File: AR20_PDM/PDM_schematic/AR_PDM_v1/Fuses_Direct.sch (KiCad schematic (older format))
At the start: 9 parts, among them U31 INA233

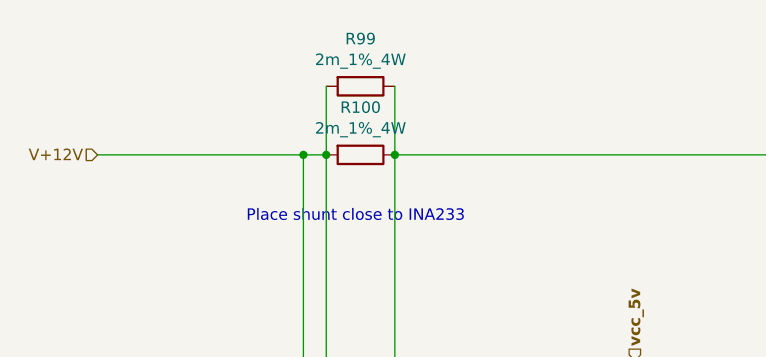
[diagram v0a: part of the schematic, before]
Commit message: Fixed wrong resistors, mos sense. Gerber files updated
- removed all R_is_protection resistors on each mosfet line
- added one R_is_protection resistors to mos_sense_all
ps, mux N-fets, does not need overvoltage protection. 60 volt tolerant.
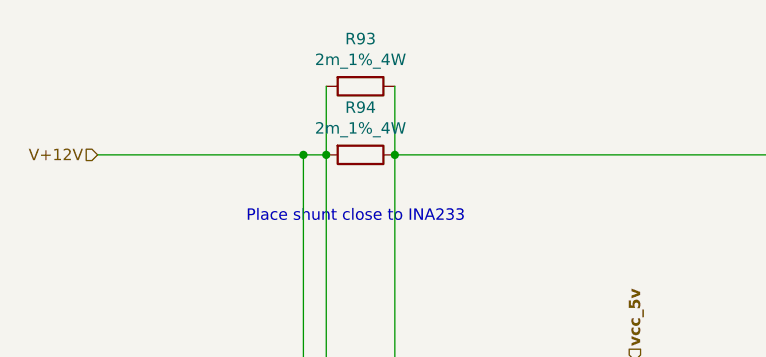
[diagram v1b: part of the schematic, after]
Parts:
- renumbered R99 to R93, R100 to R94
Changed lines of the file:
@@
 AR Path="/5E0FDCCC/5E1E306F" Ref="R?"  Part="1"
 AR Path="/5E10174B/5E1E306F" Ref="R?"  Part="1"
-AR Path="/5DE4D361/5E1E306F" Ref="R100"  Part="1"
-F 0 "R100" V 3243 3000 50  0000 C CNN
+AR Path="/5DE4D361/5E1E306F" Ref="R94"  Part="1"
+F 0 "R94" V 3243 3000 50  0000 C CNN
 F 1 "2m_1%_4W" V 3334 3000 50  0000 C CNN
 F 2 "Resistor_SMD:R_2512_6332Metric" V 3380 3000 50  0001 C CNN
@@
 AR Path="/5E0FDCCC/5E24C0CF" Ref="R?"  Part="1"
 AR Path="/5E10174B/5E24C0CF" Ref="R?"  Part="1"
-AR Path="/5DE4D361/5E24C0CF" Ref="R99"  Part="1"
-F 0 "R99" V 3243 2700 50  0000 C CNN
+AR Path="/5DE4D361/5E24C0CF" Ref="R93"  Part="1"
+F 0 "R93" V 3243 2700 50  0000 C CNN
 F 1 "2m_1%_4W" V 3334 2700 50  0000 C CNN
 F 2 "Resistor_SMD:R_2512_6332Metric" V 3380 2700 50  0001 C CNN

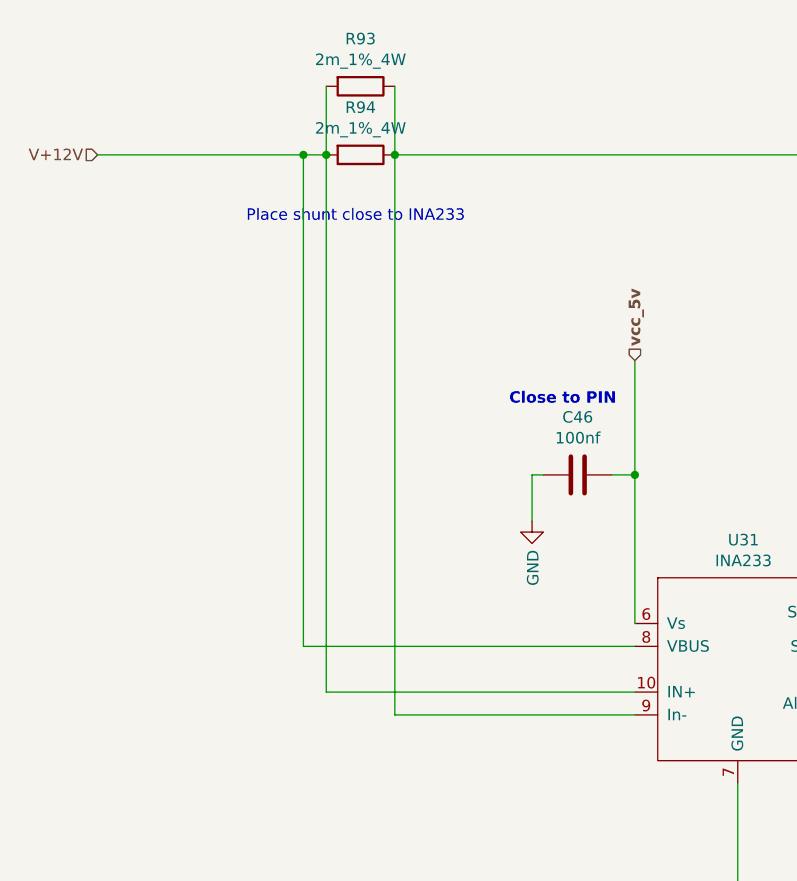
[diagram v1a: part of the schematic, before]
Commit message: Major redesign. schematics completed, PCB work in progress
-TODO : A proper changelog file. Where all changes will apear 
- Redesigned schematics to accommodate errors in the improvement list
- More detail in ALPHA improvement list
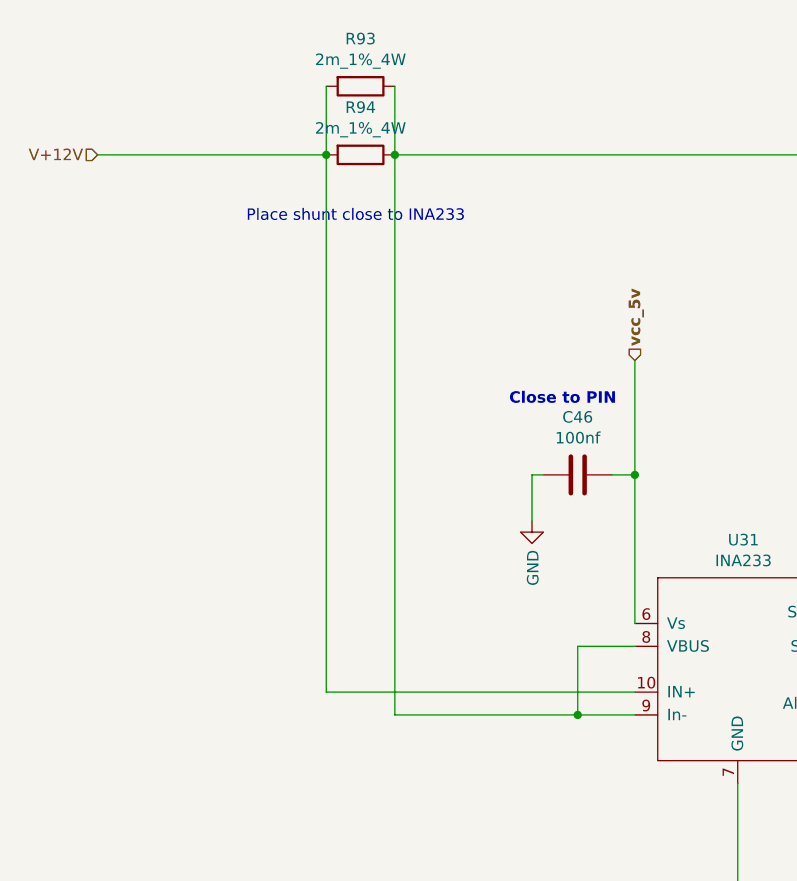
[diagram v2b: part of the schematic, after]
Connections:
- net V+12V: no longer U31.8 (VBUS)
- net at F1.2, F2.2, F3.2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: now also U31.8 (VBUS)
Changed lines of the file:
@@
 $Descr A4 11693 8268
 encoding utf-8
-Sheet 13 13
+Sheet 12 14
 Title ""
 Date ""
@@
 Place shunt close to INA233\n
 Wire Wire Line
-	2300 3000 3200 3000
-Wire Wire Line
 	5950 2650 5950 2950
 Wire Wire Line
@@
 Wire Wire Line
 	4650 5350 3300 5350
-Wire Wire Line
-	3600 5450 4650 5450
-Wire Wire Line
-	3200 5150 3200 3000
-Wire Wire Line
-	3200 5150 4650 5150
-Connection ~ 3200 3000
 Text HLabel 8950 3550 2    50   Output ~ 0
 SHUTDOWN_OUT
@@
 Connection ~ 3600 3000
 Wire Wire Line
-	3200 3000 3300 3000
-Wire Wire Line
 	3300 3000 3300 5350
 Connection ~ 3300 3000
@@
 Wire Wire Line
 	3600 3000 3600 2700
+Wire Wire Line
+	2300 3000 3300 3000
+Wire Wire Line
+	4650 5150 4400 5150
+Wire Wire Line
+	4400 5150 4400 5450
+Wire Wire Line
+	3600 5450 4400 5450
+Connection ~ 4400 5450
+Wire Wire Line
+	4400 5450 4650 5450
 $EndSCHEMATC

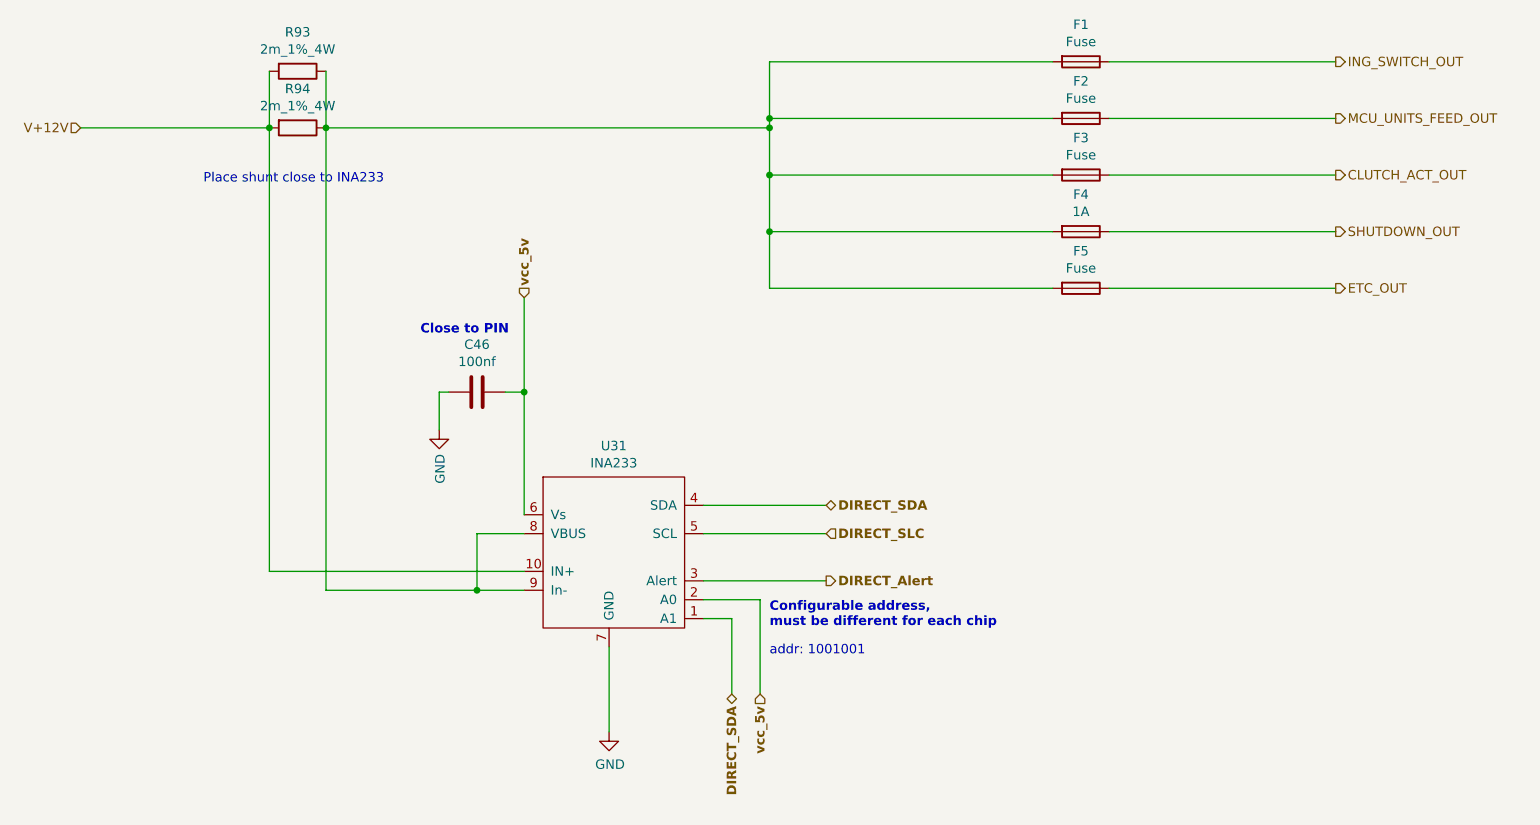
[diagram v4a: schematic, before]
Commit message: schematics rework
Fixed INA233 frying due to inductive flyback:
- Paced ina233 high side of the mosftets
- New input protection reseistors, and zener diodes, on each ina233.
Simplified:
- Removed the MUX and mos sense lines, as i realize that most of this functionality can be obtained trough INA233.
- Removed some of the cappacitors , besides the most needed ones.
- removed  back to back zener diode configuration, now a single diode insted.
 to reduce negative voltage in case of loss of VS, to be easy on the INA233 filters.
new stuff:
- Another temp sensor.
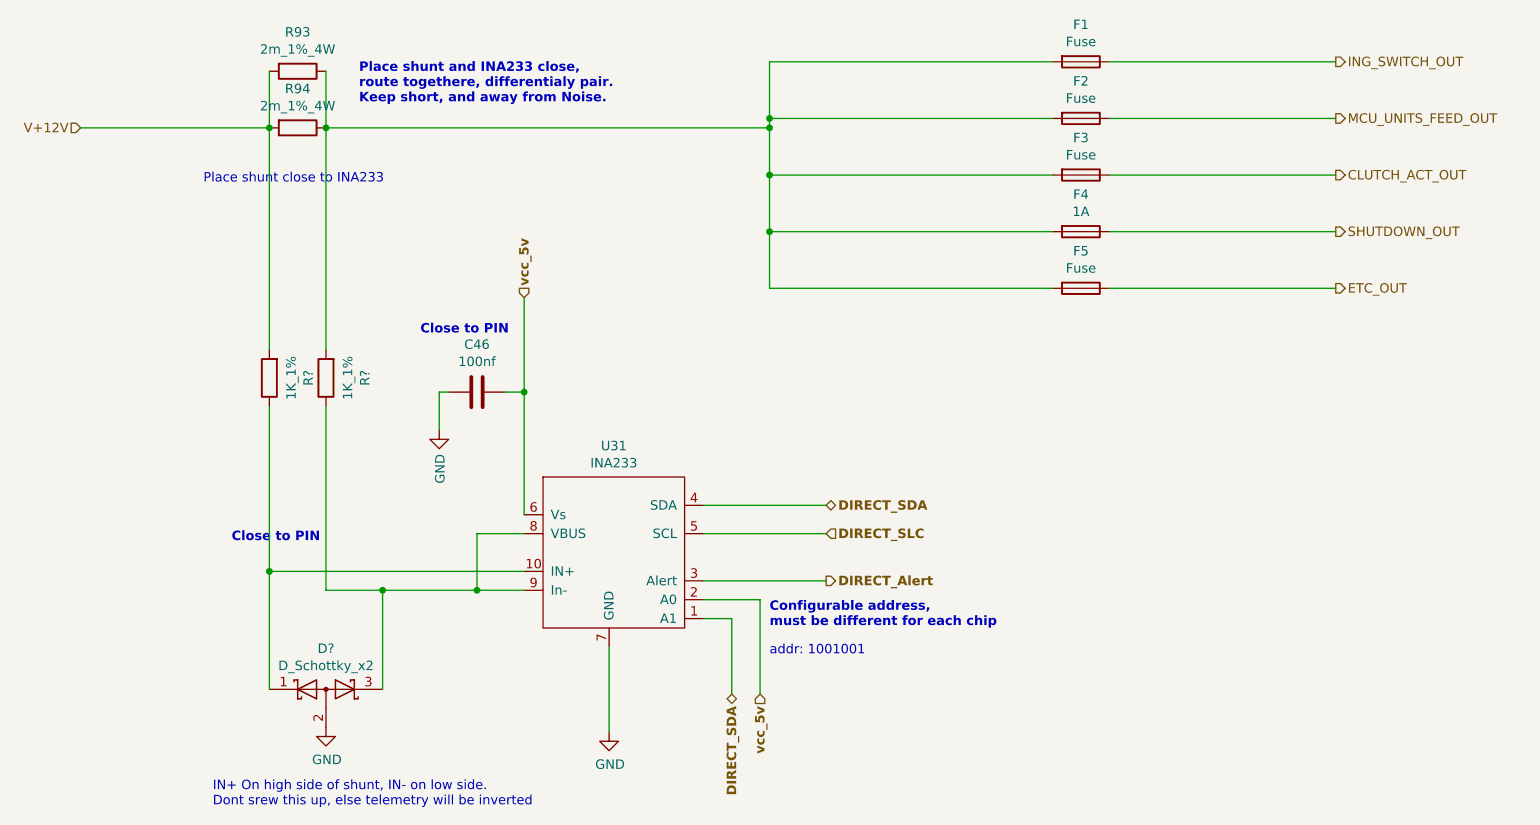
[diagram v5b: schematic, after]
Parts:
- added D?: D_Schottky_x2, symbol AR20_PDM_v1-rescue:D_Schottky_x2
- added R? (x2): 1K_1%, Resistor_SMD:R_0603_1608Metric, symbol AR20_PDM_v1-rescue:R-Device
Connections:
- net GND: now also D?.2 (A)
- net V+12V: now also R?.2; no longer U31.10 (IN+)
- net at F1.2, F2.2, F3.2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: now also R?.2; no longer U31.8 (VBUS), U31.9 (In-)
- new net: D?.1 (K), R?.1, U31.10 (IN+)
- new net: D?.3 (K), R?.1, U31.8 (VBUS), U31.9 (In-)
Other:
- note added: "IN+ On high side of shunt, IN- on low side.\nDont srew this up, else telemetry will be inverted"
- note added: "Place shunt and INA233 close, \nroute togethere, differentialy pair. \nKeep short, and away from Noise."
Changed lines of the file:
@@
 $Descr A4 11693 8268
 encoding utf-8
-Sheet 11 14
+Sheet 10 13
 Title ""
 Date ""
@@
 $EndComp
 Wire Wire Line
-	3600 3000 3600 5450
-Wire Wire Line
 	3600 3000 5950 3000
 Connection ~ 3600 3000
-Wire Wire Line
-	3300 3000 3300 5350
 Connection ~ 3300 3000
 Text Notes 5950 5800 0    50   ~ 0
@@
 	4400 5150 4400 5450
 Wire Wire Line
-	3600 5450 4400 5450
+	3600 5450 3900 5450
 Connection ~ 4400 5450
 Wire Wire Line
 	4400 5450 4650 5450
+Text Notes 3100 5200 0    50   ~ 10
+Close to PIN
+$Comp
+L AR20_PDM_v1-rescue:D_Schottky_x2 D?
+U 1 1 5EED49C1
+P 3600 5975
+AR Path="/5DA89415/5EED49C1" Ref="D?"  Part="1"
+AR Path="/5E10174B/5EED49C1" Ref="D?"  Part="1"
+F 0 "D?" H 3600 6191 50  0000 C CNN
+F 1 "D_Schottky_x2" H 3600 6100 50  0000 C CNN
+F 2 "" H 3600 5975 50  0001 C CNN
+F 3 "~" H 3600 5975 50  0001 C CNN
+	1    3600 5975
+	1    0    0    -1
+$EndComp
+$Comp
+L AR20_PDM_v1-rescue:GND-power #PWR?
+U 1 1 5EED49DB
+P 3600 6175
+AR Path="/5DA89415/5EED49DB" Ref="#PWR?"  Part="1"
+AR Path="/5DEB10A1/5EED49DB" Ref="#PWR?"  Part="1"
+AR Path="/5DEB20EA/5EED49DB" Ref="#PWR?"  Part="1"
+AR Path="/5E0E4725/5EED49DB" Ref="#PWR?"  Part="1"
+AR Path="/5E0E4A93/5EED49DB" Ref="#PWR?"  Part="1"
+AR Path="/5E0E4EB5/5EED49DB" Ref="#PWR?"  Part="1"
+AR Path="/5E0E5304/5EED49DB" Ref="#PWR?"  Part="1"
+AR Path="/5E0E594B/5EED49DB" Ref="#PWR?"  Part="1"
+AR Path="/5E0E607C/5EED49DB" Ref="#PWR?"  Part="1"
+AR Path="/5E0FB5C8/5EED49DB" Ref="#PWR?"  Part="1"
+AR Path="/5E0FBBBD/5EED49DB" Ref="#PWR?"  Part="1"
+AR Path="/5E0FC3A2/5EED49DB" Ref="#PWR?"  Part="1"
+AR Path="/5E0FCFDC/5EED49DB" Ref="#PWR?"  Part="1"
+AR Path="/5E0FDCCC/5EED49DB" Ref="#PWR?"  Part="1"
+AR Path="/5E10174B/5EED49DB" Ref="#PWR?"  Part="1"
+F 0 "#PWR?" H 3600 5925 50  0001 C CNN
+F 1 "GND" H 3605 6002 50  0000 C CNN
+F 2 "" H 3600 6175 50  0001 C CNN
+F 3 "" H 3600 6175 50  0001 C CNN
+	1    3600 6175
+	1    0    0    -1
+$EndComp
+Text Notes 3000 6600 0    50   ~ 0
+IN+ On high side of shunt, IN- on low side.\nDont srew this up, else telemetry will be inverted
+Text Notes 3775 2875 0    50   ~ 10
+Place shunt and INA233 close, \nroute togethere, differentialy pair. \nKeep short, and away from Noise.
+$Comp
+L AR20_PDM_v1-rescue:R-Device R?
+U 1 1 5EED49CD
+P 3300 4325
+AR Path="/5DA89415/5EED49CD" Ref="R?"  Part="1"
+AR Path="/5DEB10A1/5EED49CD" Ref="R?"  Part="1"
+AR Path="/5DEB20EA/5EED49CD" Ref="R?"  Part="1"
+AR Path="/5E0E4725/5EED49CD" Ref="R?"  Part="1"
+AR Path="/5E0E4A93/5EED49CD" Ref="R?"  Part="1"
+AR Path="/5E0E4EB5/5EED49CD" Ref="R?"  Part="1"
+AR Path="/5E0E5304/5EED49CD" Ref="R?"  Part="1"
+AR Path="/5E0E594B/5EED49CD" Ref="R?"  Part="1"
+AR Path="/5E0E607C/5EED49CD" Ref="R?"  Part="1"
+AR Path="/5E0FB5C8/5EED49CD" Ref="R?"  Part="1"
+AR Path="/5E0FBBBD/5EED49CD" Ref="R?"  Part="1"
+AR Path="/5E0FC3A2/5EED49CD" Ref="R?"  Part="1"
+AR Path="/5E0FCFDC/5EED49CD" Ref="R?"  Part="1"
+AR Path="/5E0FDCCC/5EED49CD" Ref="R?"  Part="1"
+AR Path="/5E10174B/5EED49CD" Ref="R?"  Part="1"
+F 0 "R?" V 3093 4325 50  0000 C CNN
+F 1 "1K_1%" V 3184 4325 50  0000 C CNN
+F 2 "Resistor_SMD:R_0603_1608Metric" V 3230 4325 50  0001 C CNN
+F 3 "~" H 3300 4325 50  0001 C CNN
+	1    3300 4325
+	-1   0    0    1
+$EndComp
+Wire Wire Line
+	3300 3000 3300 4175
+Wire Wire Line
+	3300 4475 3300 5350
+Wire Wire Line
+	3600 3000 3600 4175
+$Comp
+L AR20_PDM_v1-rescue:R-Device R?
+U 1 1 5EED49C7
+P 3600 4325
+AR Path="/5DA89415/5EED49C7" Ref="R?"  Part="1"
+AR Path="/5DEB10A1/5EED49C7" Ref="R?"  Part="1"
+AR Path="/5DEB20EA/5EED49C7" Ref="R?"  Part="1"
+AR Path="/5E0E4725/5EED49C7" Ref="R?"  Part="1"
+AR Path="/5E0E4A93/5EED49C7" Ref="R?"  Part="1"
+AR Path="/5E0E4EB5/5EED49C7" Ref="R?"  Part="1"
+AR Path="/5E0E5304/5EED49C7" Ref="R?"  Part="1"
+AR Path="/5E0E594B/5EED49C7" Ref="R?"  Part="1"
+AR Path="/5E0E607C/5EED49C7" Ref="R?"  Part="1"
+AR Path="/5E0FB5C8/5EED49C7" Ref="R?"  Part="1"
+AR Path="/5E0FBBBD/5EED49C7" Ref="R?"  Part="1"
+AR Path="/5E0FC3A2/5EED49C7" Ref="R?"  Part="1"
+AR Path="/5E0FCFDC/5EED49C7" Ref="R?"  Part="1"
+AR Path="/5E0FDCCC/5EED49C7" Ref="R?"  Part="1"
+AR Path="/5E10174B/5EED49C7" Ref="R?"  Part="1"
+F 0 "R?" V 3393 4325 50  0000 C CNN
+F 1 "1K_1%" V 3484 4325 50  0000 C CNN
+F 2 "Resistor_SMD:R_0603_1608Metric" V 3530 4325 50  0001 C CNN
+F 3 "~" H 3600 4325 50  0001 C CNN
+	1    3600 4325
+	-1   0    0    1
+$EndComp
+Wire Wire Line
+	3600 4475 3600 5450
+Wire Wire Line
+	3300 5350 3300 5975
+Connection ~ 3300 5350
+Wire Wire Line
+	3900 5975 3900 5450
+Connection ~ 3900 5450
+Wire Wire Line
+	3900 5450 4400 5450
 $EndSCHEMATC

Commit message: Working on pcb layout
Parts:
- removed D?: D_Schottky_x2, symbol AR20_PDM_v1-rescue:D_Schottky_x2
- added D61, D62: D_Schottky_BAT60A, AR_PDM_v1:D_Shotky_BAT60_HandSoldering, symbol AR20_PDM_v1-rescue:D_Schottky_BAT60A
- gave numbers to parts that had none: 2
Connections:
- net GND: now also D61.2 (A), D62.2 (A)
- net at R127.1, U31.10 (IN+): now also D61.1 (K)
- net at R128.1, U31.8 (VBUS), U31.9 (In-): now also D62.1 (K)
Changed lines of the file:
@@
 Wire Wire Line
 	4400 5150 4400 5450
-Wire Wire Line
-	3600 5450 3900 5450
 Connection ~ 4400 5450
 Wire Wire Line
@@
 Text Notes 3100 5200 0    50   ~ 10
 Close to PIN
-$Comp
-L AR20_PDM_v1-rescue:D_Schottky_x2 D?
-U 1 1 5EED49C1
-P 3600 5975
-AR Path="/5DA89415/5EED49C1" Ref="D?"  Part="1"
-AR Path="/5E10174B/5EED49C1" Ref="D?"  Part="1"
-F 0 "D?" H 3600 6191 50  0000 C CNN
-F 1 "D_Schottky_x2" H 3600 6100 50  0000 C CNN
-F 2 "" H 3600 5975 50  0001 C CNN
-F 3 "~" H 3600 5975 50  0001 C CNN
-	1    3600 5975
-	1    0    0    -1
-$EndComp
-$Comp
-L AR20_PDM_v1-rescue:GND-power #PWR?
-U 1 1 5EED49DB
-P 3600 6175
-AR Path="/5DA89415/5EED49DB" Ref="#PWR?"  Part="1"
-AR Path="/5DEB10A1/5EED49DB" Ref="#PWR?"  Part="1"
-AR Path="/5DEB20EA/5EED49DB" Ref="#PWR?"  Part="1"
-AR Path="/5E0E4725/5EED49DB" Ref="#PWR?"  Part="1"
-AR Path="/5E0E4A93/5EED49DB" Ref="#PWR?"  Part="1"
-AR Path="/5E0E4EB5/5EED49DB" Ref="#PWR?"  Part="1"
-AR Path="/5E0E5304/5EED49DB" Ref="#PWR?"  Part="1"
-AR Path="/5E0E594B/5EED49DB" Ref="#PWR?"  Part="1"
-AR Path="/5E0E607C/5EED49DB" Ref="#PWR?"  Part="1"
-AR Path="/5E0FB5C8/5EED49DB" Ref="#PWR?"  Part="1"
-AR Path="/5E0FBBBD/5EED49DB" Ref="#PWR?"  Part="1"
-AR Path="/5E0FC3A2/5EED49DB" Ref="#PWR?"  Part="1"
-AR Path="/5E0FCFDC/5EED49DB" Ref="#PWR?"  Part="1"
-AR Path="/5E0FDCCC/5EED49DB" Ref="#PWR?"  Part="1"
-AR Path="/5E10174B/5EED49DB" Ref="#PWR?"  Part="1"
-F 0 "#PWR?" H 3600 5925 50  0001 C CNN
-F 1 "GND" H 3605 6002 50  0000 C CNN
-F 2 "" H 3600 6175 50  0001 C CNN
-F 3 "" H 3600 6175 50  0001 C CNN
-	1    3600 6175
-	1    0    0    -1
-$EndComp
 Text Notes 3000 6600 0    50   ~ 0
 IN+ On high side of shunt, IN- on low side.\nDont srew this up, else telemetry will be inverted
@@
 AR Path="/5E0FDCCC/5EED49CD" Ref="R?"  Part="1"
 AR Path="/5E10174B/5EED49CD" Ref="R?"  Part="1"
-F 0 "R?" V 3093 4325 50  0000 C CNN
+AR Path="/5DE4D361/5EED49CD" Ref="R127"  Part="1"
+F 0 "R127" V 3093 4325 50  0000 C CNN
 F 1 "1K_1%" V 3184 4325 50  0000 C CNN
 F 2 "Resistor_SMD:R_0603_1608Metric" V 3230 4325 50  0001 C CNN
@@
 AR Path="/5E0FDCCC/5EED49C7" Ref="R?"  Part="1"
 AR Path="/5E10174B/5EED49C7" Ref="R?"  Part="1"
-F 0 "R?" V 3393 4325 50  0000 C CNN
+AR Path="/5DE4D361/5EED49C7" Ref="R128"  Part="1"
+F 0 "R128" V 3393 4325 50  0000 C CNN
 F 1 "1K_1%" V 3484 4325 50  0000 C CNN
 F 2 "Resistor_SMD:R_0603_1608Metric" V 3530 4325 50  0001 C CNN
@@
 	3600 4475 3600 5450
 Wire Wire Line
-	3300 5350 3300 5975
+	3600 5450 3750 5450
+$Comp
+L AR20_PDM_v1-rescue:D_Schottky_BAT60A D?
+U 1 1 5EFED613
+P 3350 5925
+AR Path="/5DA89415/5EFED613" Ref="D?"  Part="1"
+AR Path="/5DE4D361/5EFED613" Ref="D61"  Part="1"
+F 0 "D61" V 3180 6035 50  0000 L CNN
+F 1 "D_Schottky_BAT60A" V 3271 6035 50  0000 L CNN
+F 2 "AR_PDM_v1:D_Shotky_BAT60_HandSoldering" H 3450 5875 50  0001 C CNN
+F 3 "~" H 3450 5875 50  0001 C CNN
+	1    3350 5925
+	0    1    1    0
+$EndComp
+$Comp
+L AR20_PDM_v1-rescue:GND-power #PWR?
+U 1 1 5EFED619
+P 3525 6100
+AR Path="/5DA89415/5EFED619" Ref="#PWR?"  Part="1"
+AR Path="/5DEB10A1/5EFED619" Ref="#PWR?"  Part="1"
+AR Path="/5DEB20EA/5EFED619" Ref="#PWR?"  Part="1"
+AR Path="/5E0E4725/5EFED619" Ref="#PWR?"  Part="1"
+AR Path="/5E0E4A93/5EFED619" Ref="#PWR?"  Part="1"
+AR Path="/5E0E4EB5/5EFED619" Ref="#PWR?"  Part="1"
+AR Path="/5E0E5304/5EFED619" Ref="#PWR?"  Part="1"
+AR Path="/5E0E594B/5EFED619" Ref="#PWR?"  Part="1"
+AR Path="/5E0E607C/5EFED619" Ref="#PWR?"  Part="1"
+AR Path="/5E0FB5C8/5EFED619" Ref="#PWR?"  Part="1"
+AR Path="/5E0FBBBD/5EFED619" Ref="#PWR?"  Part="1"
+AR Path="/5E0FC3A2/5EFED619" Ref="#PWR?"  Part="1"
+AR Path="/5E0FCFDC/5EFED619" Ref="#PWR?"  Part="1"
+AR Path="/5E0FDCCC/5EFED619" Ref="#PWR?"  Part="1"
+AR Path="/5E10174B/5EFED619" Ref="#PWR?"  Part="1"
+AR Path="/5DE4D361/5EFED619" Ref="#PWR030"  Part="1"
+F 0 "#PWR030" H 3525 5850 50  0001 C CNN
+F 1 "GND" H 3530 5927 50  0000 C CNN
+F 2 "" H 3525 6100 50  0001 C CNN
+F 3 "" H 3525 6100 50  0001 C CNN
+	1    3525 6100
+	1    0    0    -1
+$EndComp
+$Comp
+L AR20_PDM_v1-rescue:D_Schottky_BAT60A D?
+U 1 1 5EFED61F
+P 3800 5925
+AR Path="/5DA89415/5EFED61F" Ref="D?"  Part="1"
+AR Path="/5DE4D361/5EFED61F" Ref="D62"  Part="1"
+F 0 "D62" V 3630 6035 50  0000 L CNN
+F 1 "D_Schottky_BAT60A" V 3721 6035 50  0000 L CNN
+F 2 "AR_PDM_v1:D_Shotky_BAT60_HandSoldering" H 3900 5875 50  0001 C CNN
+F 3 "~" H 3900 5875 50  0001 C CNN
+	1    3800 5925
+	0    1    1    0
+$EndComp
+Wire Wire Line
+	3750 5625 3750 5450
+Wire Wire Line
+	3300 5975 3525 5975
+Wire Wire Line
+	3525 6100 3525 5975
+Connection ~ 3525 5975
+Wire Wire Line
+	3525 5975 3750 5975
+Connection ~ 3750 5450
+Wire Wire Line
+	3750 5450 4400 5450
+Wire Wire Line
+	3300 5350 3300 5625
 Connection ~ 3300 5350
-Wire Wire Line
-	3900 5975 3900 5450
-Connection ~ 3900 5450
-Wire Wire Line
-	3900 5450 4400 5450
 $EndSCHEMATC
